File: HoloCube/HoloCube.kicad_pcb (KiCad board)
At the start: 2 copper layers, 19 parts, among them J1 ESPProgUART_RX, J3 USB_C_Receptacle_USB2.0, U1 ESP32-PICO-D4, U2 LIS2DE12, U4 XC6209

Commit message: Place Parts
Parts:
- removed D2, D4: LED, LED_SMD:LED_0603_1608Metric
- added C1: 10uf, Capacitor_SMD:C_0603_1608Metric, F.Cu at (206.5, 111.0)
- added C2: 0.1uf, Capacitor_SMD:C_0603_1608Metric, F.Cu at (211.4, 110.9)
- added C4: 0.1uf, Capacitor_SMD:C_0603_1608Metric, F.Cu at (199.5, 116.0)
- added C7: TBD, Capacitor_SMD:C_0603_1608Metric, F.Cu at (209.2, 109.0)
- added C8: 10pf, Capacitor_SMD:C_0603_1608Metric, F.Cu at (203.9, 110.1)
- added C9: TBD, Capacitor_SMD:C_0603_1608Metric, F.Cu at (201.0, 109.0)
- added J2: Conn_01x08_MountingPin, Connector_FFC-FPC:TE_0-1734839-8_1x08-1MP_P0.5mm_Horizontal, F.Cu at (215.7, 113.7)
- added J4: Micro_SD_Card, KisonNew:C91145, B.Cu at (205.3, 115.8)
- added J5: ESPProgJTAG_RX, KisonNew:IDC_1.27mm_10P, F.Cu at (193.8, 114.8)
- added JP1: Jumper, Resistor_SMD:R_0603_1608Metric, F.Cu at (199.5, 112.8)
- added JP2: Jumper, Resistor_SMD:R_0603_1608Metric, F.Cu at (199.3, 119.8)
- added R10: 10k, Resistor_SMD:R_0603_1608Metric, B.Cu at (216.4, 115.6)
- added R11: 0, Resistor_SMD:R_0603_1608Metric, B.Cu at (198.8, 124.8)
- added R12: 100k, Resistor_SMD:R_0603_1608Metric, F.Cu at (202.3, 113.2)
- added R13: 100k, Resistor_SMD:R_0603_1608Metric, F.Cu at (197.6, 119.8)
- added R14: 10k, Resistor_SMD:R_0603_1608Metric, B.Cu at (200.4, 124.8)
- added R15: 10k, Resistor_SMD:R_0603_1608Metric, B.Cu at (200.5, 128.1)
- added R16: 10k, Resistor_SMD:R_0603_1608Metric, B.Cu at (202.4, 124.8)
- added R17: 10k, Resistor_SMD:R_0603_1608Metric, B.Cu at (202.4, 128.1)
- added R2: 0, Resistor_SMD:R_0603_1608Metric, B.Cu at (195.0, 109.7)
- added R3: 0, Resistor_SMD:R_0603_1608Metric, F.Cu at (218.9, 127.7)
- added R9: 10k, Resistor_SMD:R_0603_1608Metric, F.Cu at (202.0, 120.6)
- added U3: BH1750FVI-TR, BH1750FVI-TR:XDCR_BH1750FVI-TR, F.Cu at (202.3, 118.7)
- C3, R1, R4, R6, R7: moved to B.Cu
- R5, R8: value 10k -> 3.3k; moved to B.Cu
- U2: value LIS2DE12 -> LIS2DH12TR; footprint Package_LGA:LGA-12_2x2mm_P0.5mm -> LIS2DH12TR:PQFN50P200X200100-12N
- moved D3 67.7 mm to (216.8, 120.8), turned to 180 degrees
- moved J3 66.5 mm to (208.8, 127.3)
- moved C6 66.0 mm to (218.9, 124.6), turned to -90 degrees
- moved U4 62.3 mm to (216.1, 125.1), turned to 90 degrees
- moved C5 59.4 mm to (215.8, 128.3), turned to 180 degrees
- moved R7 58.9 mm to (211.6, 126.8), turned to 90 degrees
- moved R6 54.9 mm to (206.2, 127.0), turned to 90 degrees
- moved R4 54.9 mm to (208.8, 128.6), turned to 180 degrees
- moved AE1 53.0 mm to (206.1, 107.3)
- moved R8 46.2 mm to (195.5, 122.3), turned to 180 degrees
- moved U2 46.0 mm to (202.4, 115.7), turned to 90 degrees
- moved R5 41.6 mm to (195.5, 119.8), turned to 180 degrees
- moved C3 40.3 mm to (191.7, 111.5), turned to 180 degrees
- moved R1 39.6 mm to (195.0, 111.5), turned to 180 degrees
- moved U1 38.2 mm to (208.8, 116.1)
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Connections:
- C5 pad 1: /EXT_5V -> +5V
- D1 pad 1: unconnected-(D1-Pad1) -> +5V
- D1 pad 3: unconnected-(D1-Pad3) -> GND
- D1 pad 4: unconnected-(D1-Pad4) -> /IO27
- D3 pad 1: /EXT_5V -> +5V
- J1 pad 6: unconnected-(J1-Pad6) -> /IO0
- R5 pad 1: /EXT_5V -> +3V3
- R5 pad 2: Net-(D2-Pad2) -> /I2C_SCL
- R8 pad 2: Net-(D4-Pad2) -> /I2C_SDA
- U1 pad 12: unconnected-(U1-Pad12) -> /I2C_SDA
- U1 pad 13: unconnected-(U1-Pad13) -> /I2C_SCL
- U1 pad 14: unconnected-(U1-Pad14) -> /IO25
- U1 pad 15: unconnected-(U1-Pad15) -> /IO26
- U1 pad 16: unconnected-(U1-Pad16) -> /IO27
- U1 pad 17: unconnected-(U1-Pad17) -> /TMS
- U1 pad 18: unconnected-(U1-Pad18) -> /TDI
- U1 pad 2: Net-(AE1-Pad1) -> Net-(U1-Pad2)
- U1 pad 20: unconnected-(U1-Pad20) -> /TCLK
- U1 pad 21: unconnected-(U1-Pad21) -> /TDO
- U1 pad 22: /TX -> /DC
- U1 pad 23: unconnected-(U1-Pad23) -> /IO0
- U1 pad 24: unconnected-(U1-Pad24) -> /IO4
- U1 pad 34: unconnected-(U1-Pad34) -> /IO5
- U1 pad 35: unconnected-(U1-Pad35) -> /IO18
- U1 pad 36: unconnected-(U1-Pad36) -> /IO23
- U1 pad 38: unconnected-(U1-Pad38) -> /IO19
- U1 pad 39: unconnected-(U1-Pad39) -> /IO22
- U1 pad 41: unconnected-(U1-Pad41) -> /TX
- U1 pad 42: unconnected-(U1-Pad42) -> /IO21
- U2 pad 1: unconnected-(U2-Pad1) -> /I2C_SCL
- U2 pad 10: unconnected-(U2-Pad10) -> +3V3
- U2 pad 2: unconnected-(U2-Pad2) -> +3V3
- U2 pad 3: unconnected-(U2-Pad3) -> Net-(JP1-Pad2)
- U2 pad 4: unconnected-(U2-Pad4) -> /I2C_SDA
- U2 pad 5: unconnected-(U2-Pad5) -> GND
- U2 pad 6: unconnected-(U2-Pad6) -> GND
- U2 pad 7: unconnected-(U2-Pad7) -> GND
- U2 pad 8: unconnected-(U2-Pad8) -> GND
- U2 pad 9: unconnected-(U2-Pad9) -> +3V3
- U4 pad 1: /EXT_5V -> +5V
- U4 pad 3: /EXT_5V -> +5V
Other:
- board outline added: 60.4 x 50 mm
- copper layers 2 -> 4

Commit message: Random Version 0.0
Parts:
- removed C4: 0.1uf, Capacitor_SMD:C_0603_1608Metric
- removed J5: ESPProgJTAG_RX, KisonNew:IDC_1.27mm_10P
- removed JP2: Jumper, Resistor_SMD:R_0603_1608Metric
- removed R10, R9: 10k, Resistor_SMD:R_0603_1608Metric
- removed R13: 100k, Resistor_SMD:R_0603_1608Metric
- removed R3: 0, Resistor_SMD:R_0603_1608Metric
- removed U3: BH1750FVI-TR, BH1750FVI-TR:XDCR_BH1750FVI-TR
- C2, C3, C5, C6, C7, C8, C9: footprint Capacitor_SMD:C_0603_1608Metric -> Capacitor_SMD:C_0402_1005Metric
- JP1, R1, R11, R12, R14, R15, R16, R17, R2, R4, R6, R7: footprint Resistor_SMD:R_0603_1608Metric -> Resistor_SMD:R_0402_1005Metric
- R5, R8: footprint Resistor_SMD:R_0603_1608Metric -> Resistor_SMD:R_0402_1005Metric; moved to F.Cu
- moved R17 14.0 mm to (215.5, 123.1), turned to 180 degrees
- moved J1 11.6 mm to (195.8, 114.4), turned to -90 degrees
- moved R8 11.1 mm to (203.4, 114.5), turned to -90 degrees
- moved R15 9.46 mm to (209.5, 125.3), turned to 90 degrees
- moved R5 8.35 mm to (203.3, 116.8), turned to -90 degrees
- moved C7 8.17 mm to (201.4, 111.3), turned to 0 degrees
- moved R2 8.00 mm to (193.8, 117.6), turned to 90 degrees
- moved R1 7.40 mm to (195.8, 118.9)
- moved C3 6.88 mm to (195.8, 117.0)
- moved R16 5.66 mm to (208.0, 125.4)
- moved J4 4.38 mm to (209.7, 115.5)
- moved JP1 4.25 mm to (201.0, 116.8)
- moved C5 3.68 mm to (216.8, 124.7)
- moved R12 3.60 mm to (202.1, 116.8), turned to -90 degrees
- moved C6 2.79 mm to (218.7, 127.3), turned to 90 degrees
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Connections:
- AE1 pad 2: (no net) -> GND
- C1 pad 1: +3.3VA -> +3V3
- C2 pad 1: +3.3VA -> +3V3
- D1 pad 4: /IO27 -> /IO19
- J2 pad 1: /IO5 -> /IO22
- J2 pad 3: /IO23 -> /IO5
- J4 pad 2: /IO21 -> /IO15
- J4 pad 3: /IO25 -> /IO13
- J4 pad 5: /IO19 -> /IO26
- J4 pad 7: /IO26 -> /IO25
- R14 pad 2: /IO26 -> /IO25
- R15 pad 2: /IO25 -> /IO13
- R16 pad 2: /IO19 -> /IO26
- R17 pad 2: /IO21 -> /IO15
- R2 pad 1: Net-(J1-Pad2) -> +3V3
- R2 pad 2: +3V3 -> Net-(J1-Pad2)
- U1 pad 1: +3.3VA -> +3V3
- U1 pad 18: /TDI -> /IO12
- U1 pad 19: +3.3VA -> +3V3
- U1 pad 20: /TCLK -> /IO13
- U1 pad 21: /TDO -> /IO15
- U1 pad 22: /DC -> unconnected-(U1-Pad22)
- U1 pad 3: +3.3VA -> +3V3
- U1 pad 36: /IO23 -> /DC
- U1 pad 37: +3.3VA -> +3V3
- U1 pad 4: +3.3VA -> +3V3
- U1 pad 42: /IO21 -> unconnected-(U1-Pad42)
- U1 pad 43: +3.3VA -> +3V3
- U1 pad 46: +3.3VA -> +3V3
- U2 pad 6: GND -> unconnected-(U2-Pad6)
- U2 pad 7: GND -> unconnected-(U2-Pad7)
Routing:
- net +3V3: track 0.00 -> 99.4 mm, vias 0 -> 9
- net GND: track 0.00 -> 73.0 mm, vias 0 -> 11
- net +5V: track 0.00 -> 52.4 mm, vias 0 -> 2
- net /IO0: track 0.00 -> 25.7 mm, vias 0 -> 2
- net /IO19: track 0.00 -> 24.2 mm, vias 0 -> 2
- net Net-(D3-Pad2): track 0.00 -> 23.7 mm, vias 0 -> 2
- net Net-(J3-PadS1): track 0.00 -> 18.4 mm
- net /RX: track 0.00 -> 17.1 mm, vias 0 -> 2
- net /IO22: track 0.00 -> 15.4 mm, vias 0 -> 2
- net /TX: track 0.00 -> 15.0 mm, vias 0 -> 2
- net /EN: track 0.00 -> 14.5 mm, vias 0 -> 2
- net /I2C_SCL: track 0.00 -> 9.69 mm
- net /IO15: track 0.00 -> 7.84 mm, vias 0 -> 1
- net Net-(AE1-Pad1): track 0.00 -> 7.36 mm
- net /IO4: track 0.00 -> 7.13 mm
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- added copper zone on B.Cu, net GND
- added copper zone on F.Cu, net GND
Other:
- board outline removed

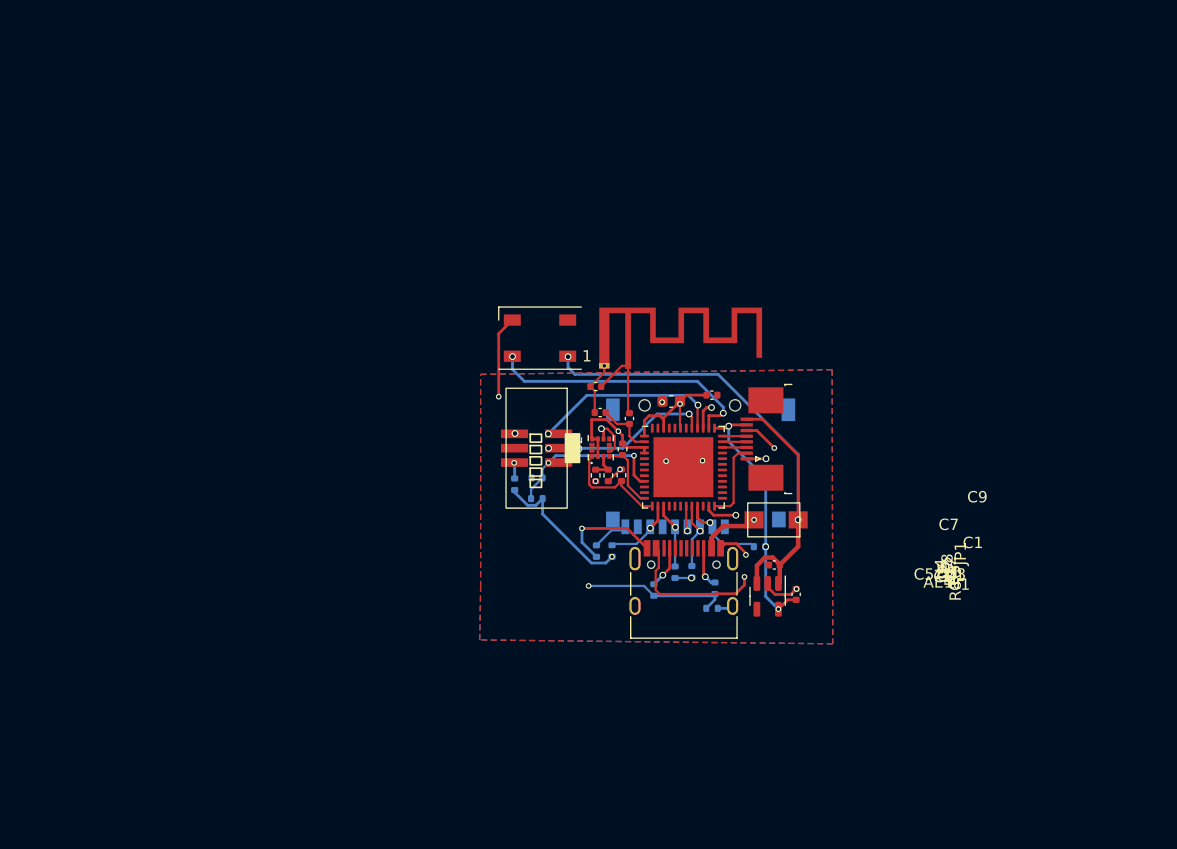
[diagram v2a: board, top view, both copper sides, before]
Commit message: Improve According to t123yh
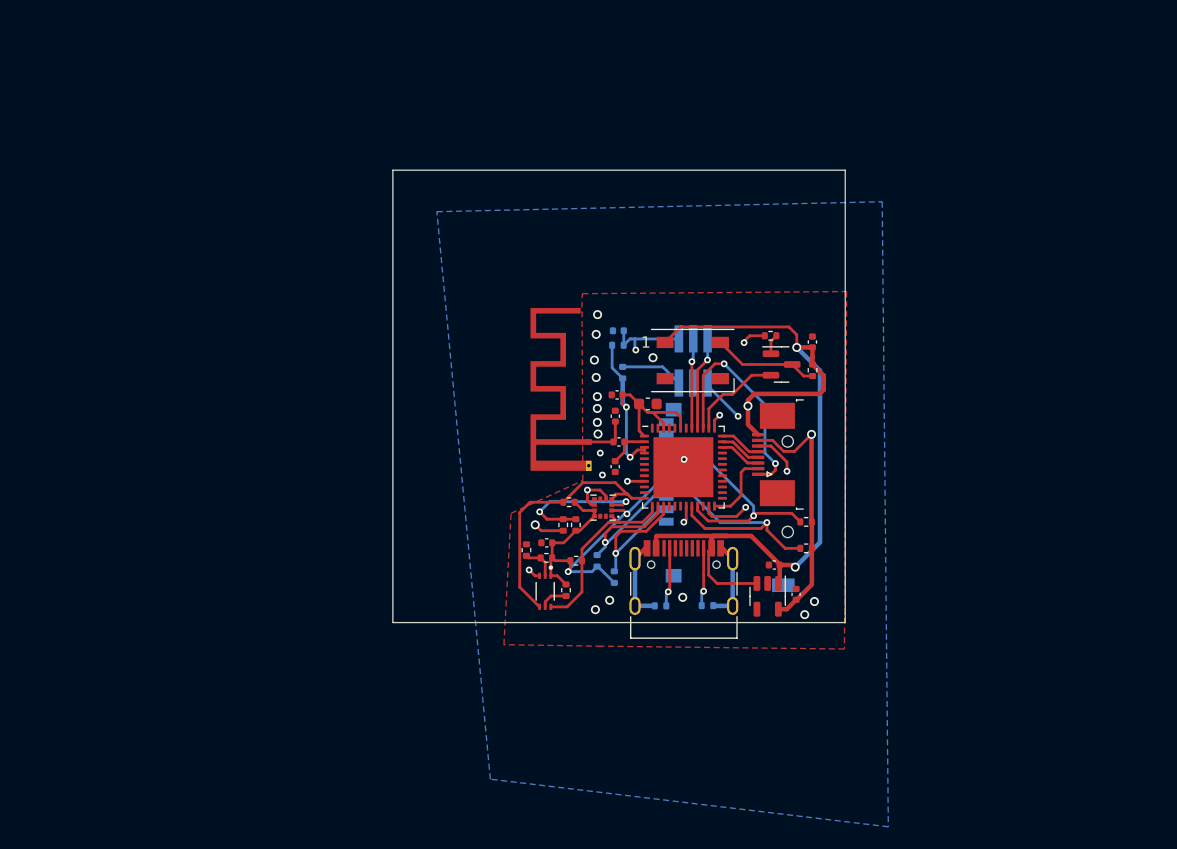
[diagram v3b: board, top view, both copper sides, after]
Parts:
- removed D3: D, KisonNew:C8678
- removed R11: 0, Resistor_SMD:R_0402_1005Metric
- added C10: 0.1uF, Capacitor_SMD:C_0402_1005Metric, F.Cu at (220.2, 105.0)
- added C4: 0.1uf, Capacitor_SMD:C_0402_1005Metric, F.Cu at (196.7, 122.8)
- added JP2: Jumper, Resistor_SMD:R_0402_1005Metric, F.Cu at (196.7, 124.1)
- added Q1: MMBT3904, Package_TO_SOT_SMD:SOT-23, F.Cu at (217.4, 107.0)
- added R10: 10k, Resistor_SMD:R_0402_1005Metric, F.Cu at (220.2, 107.5)
- added R3: 10k, Resistor_SMD:R_0402_1005Metric, F.Cu at (198.4, 127.0)
- added R9: 100k, Resistor_SMD:R_0402_1005Metric, F.Cu at (194.9, 123.4)
- added U3: BH1750FVI-TR, BH1750FVI-TR:XDCR_BH1750FVI-TR, F.Cu at (196.5, 127.1)
- J1: moved to B.Cu
- R14, R16: moved to F.Cu
- R4: value 0 -> 1.5k; moved to F.Cu
- moved R4 24.7 mm to (216.5, 104.5)
- moved R14 17.4 mm to (219.6, 120.9), turned to 180 degrees
- moved J1 15.9 mm to (209.6, 106.7), turned to 180 degrees
- moved R1 15.3 mm to (203.0, 105.3), turned to 0 degrees
- moved C3 14.9 mm to (203.0, 104.0)
- moved R2 13.7 mm to (203.4, 107.7)
- moved D1 13.7 mm to (209.6, 106.7), turned to 0 degrees
- moved R17 13.1 mm to (202.7, 125.8), turned to 90 degrees
- moved R16 11.8 mm to (219.6, 123.3), turned to 180 degrees
- moved R5 8.55 mm to (199.3, 124.4), turned to 0 degrees
- moved R15 8.44 mm to (201.1, 124.4)
- moved C2 8.38 mm to (202.9, 109.7), turned to 180 degrees
- moved AE1 7.58 mm to (200.4, 113.9), turned to 90 degrees
- moved R8 6.65 mm to (198.7, 119.2), turned to 180 degrees
- moved U2 5.31 mm to (201.7, 119.7), turned to 180 degrees
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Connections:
- D1 pad 4: /IO19 -> Net-(D1-Pad4)
- J3 pad A4: Net-(D3-Pad2) -> +5V
- J3 pad A9: Net-(D3-Pad2) -> +5V
- J3 pad B4: Net-(D3-Pad2) -> +5V
- J3 pad B9: Net-(D3-Pad2) -> +5V
- J3 pad S1: Net-(J3-PadS1) -> GND
- J4 pad 2: /IO15 -> /IO26
- J4 pad 3: /IO13 -> /IO25
- J4 pad 5: /IO26 -> /IO13
- J4 pad 7: /IO25 -> /IO15
- J4 pad 9: Net-(J4-Pad9) -> GND
- R14 pad 2: /IO25 -> /IO15
- R15 pad 2: /IO13 -> /IO25
- R16 pad 2: /IO26 -> /IO13
- R17 pad 2: /IO15 -> /IO26
- R4 pad 1: Net-(J3-PadS1) -> Net-(Q1-Pad1)
- R4 pad 2: GND -> +3V3
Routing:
- net GND: track 73.0 -> 26.4 mm, vias 11 -> 21
- net +3V3: track 99.4 -> 132.9 mm, vias 9 -> 8
- net +5V: track 52.4 -> 76.6 mm, vias 2 -> 3
- net Net-(D3-Pad2): track 23.7 -> 0.00 mm, vias 2 -> 0
- net Net-(J3-PadS1): track 18.4 -> 0.00 mm
- net /I2C_SDA: track 6.05 -> 23.4 mm
- net /IO13: track 5.89 -> 23.2 mm
- net /IO19: track 24.2 -> 8.44 mm, vias 2 -> 0
- net /IO15: track 7.84 -> 21.2 mm
- net Net-(JP1-Pad2): track 2.47 -> 12.9 mm, vias 0 -> 2
- net Net-(D1-Pad4): track 0.00 -> 9.37 mm
- net /IO26: track 5.77 -> 15.1 mm
- net /IO25: track 6.33 -> 15.4 mm
- net /IO0: track 25.7 -> 16.8 mm
- net /RX: track 17.1 -> 8.26 mm, vias 2 -> 1
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- added copper zone on In1.Cu, net GND
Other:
- board outline added: 40 x 40 mm
- board text added: "emm这玩意怎么铺铜的时候连上2脚啊，因为天线的net2脚设为GND也铺不到"
- board text added: "朝向用户"
- board text added: "这边是屁股，记得机械在光传感器上留出透明位置"

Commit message: Improve again
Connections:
- J2 pad MP: unconnected-(J2-PadMP) -> GND
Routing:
- net GND: track 26.4 -> 31.4 mm, vias 21 -> 25

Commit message: V0.1
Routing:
- net GND: vias 25 -> 27
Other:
- board size 40 x 40 mm -> 30 x 29 mm
- board text added: "定位孔相距16mm,右边孔相距上下左右边线2mm"
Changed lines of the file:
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@@
     )
   )
-  (gr_line (start 183.07 129.83) (end 223.07 129.83) (layer "Edge.Cuts") (width 0.1))
-  (gr_line (start 223.07 89.83) (end 223.07 129.83) (layer "Edge.Cuts") (width 0.1))
-  (gr_line (start 223.07 89.83) (end 183.07 89.83) (layer "Edge.Cuts") (width 0.1))
-  (gr_line (start 183.07 129.83) (end 183.07 89.83) (layer "Edge.Cuts") (width 0.1))
+  (gr_line (start 194.57 129.79) (end 221.57 129.79) (layer "Edge.Cuts") (width 0.1))
+  (gr_arc (start 221.57 100.79) (mid 222.63066 101.22934) (end 223.07 102.29) (layer "Edge.Cuts") (width 0.1))
+  (gr_arc (start 194.57 129.79) (mid 193.50934 129.35066) (end 193.07 128.29) (layer "Edge.Cuts") (width 0.1))
+  (gr_line (start 193.07 128.29) (end 193.07 102.29) (layer "Edge.Cuts") (width 0.1))
+  (gr_line (start 223.07 102.29) (end 223.07 128.29) (layer "Edge.Cuts") (width 0.1))
+  (gr_arc (start 223.07 128.29) (mid 222.63066 129.35066) (end 221.57 129.79) (layer "Edge.Cuts") (width 0.1))
+  (gr_arc (start 193.07 102.29) (mid 193.50934 101.22934) (end 194.57 100.79) (layer "Edge.Cuts") (width 0.1))
+  (gr_line (start 221.57 100.79) (end 194.57 100.79) (layer "Edge.Cuts") (width 0.1))
   (gr_text "这边是屁股，记得机械在光传感器上留出透明位置" (at 208.71 134.04) (layer "Cmts.User")
     (effects (font (size 1 1) (thickness 0.15)))
@@
   (gr_text "朝向用户" (at 208.91 99.25) (layer "Cmts.User")
     (effects (font (size 1 1) (thickness 0.15)))
+  )
+  (gr_text "定位孔相距16mm,右边孔相距上下左右边线2mm" (at 211.52 96.33) (layer "Cmts.User")
+    (effects (font (size 1.5 1.5) (thickness 0.3)))
   )
   (gr_text "emm这玩意怎么铺铜的时候连上2脚啊，因为天线的net2脚设为GND也铺不到" (at 201.98 88.91) (layer "Cmts.User")
@@
   (segment (start 201.6 116.78) (end 201.21 116.78) (width 0.6) (layer "F.Cu") (net 3))
   (via (at 208.7 127.6) (size 0.8) (drill 0.5) (layers "F.Cu" "B.Cu") (free) (net 3))
+  (via (at 221.07 102.79) (size 1.5) (drill 1) (layers "F.Cu" "B.Cu") (free) (net 3))
   (via (at 201.15 112.13) (size 0.8) (drill 0.5) (layers "F.Cu" "B.Cu") (free) (net 3))
   (via (at 217.92 116.45) (size 0.6) (drill 0.3) (layers "F.Cu" "B.Cu") (net 3))
@@
   (via (at 208.82 115.4) (size 0.6) (drill 0.3) (layers "F.Cu" "B.Cu") (net 3))
   (via (at 201.05 104.35) (size 0.8) (drill 0.5) (layers "F.Cu" "B.Cu") (free) (net 3))
+  (via (at 205.07 102.79) (size 1.5) (drill 1) (layers "F.Cu" "B.Cu") (free) (net 3))
   (via (at 210.7184 117.5512) (size 0.8) (drill 0.5) (layers "F.Cu" "B.Cu") (net 3))
   (via (at 201.15 110.9) (size 0.8) (drill 0.5) (layers "F.Cu" "B.Cu") (free) (net 3))
@@
   (segment (start 202.75 118.5925) (end 202.4225 118.92) (width 0.25) (layer "F.Cu") (net 16))
   (segment (start 203.76 118.47) (end 203.832482 118.47) (width 0.25) (layer "F.Cu") (net 16))
+  (segment (start 196.04 127.65904) (end 194.28548 125.90452) (width 0.25) (layer "F.Cu") (net 16))
   (segment (start 202.75 118.47) (end 202.75 118.5925) (width 0.25) (layer "F.Cu") (net 16))
+  (segment (start 196.04 128.445) (end 196.04 127.65904) (width 0.25) (layer "F.Cu") (net 16))
   (segment (start 203.832482 118.47) (end 204.202482 118.84) (width 0.25) (layer "F.Cu") (net 16))
   (segment (start 194.28548 120.10452) (end 195.2 119.19) (width 0.25) (layer "F.Cu") (net 16))
   (segment (start 195.2 119.19) (end 198.14 119.19) (width 0.25) (layer "F.Cu") (net 16))
+  (segment (start 194.28548 125.90452) (end 194.28548 120.10452) (width 0.25) (layer "F.Cu") (net 16))
   (segment (start 204.202482 118.84) (end 205.31 118.84) (width 0.25) (layer "F.Cu") (net 16))
-  (segment (start 196.04 128.445) (end 194.28548 126.69048) (width 0.25) (layer "F.Cu") (net 16))
   (segment (start 198.14 119.19) (end 199.87 117.46) (width 0.25) (layer "F.Cu") (net 16))
   (segment (start 202.75 117.46) (end 203.76 118.47) (width 0.25) (layer "F.Cu") (net 16))
-  (segment (start 194.28548 126.69048) (end 194.28548 120.10452) (width 0.25) (layer "F.Cu") (net 16))
   (segment (start 203.832482 118.47) (end 202.75 118.47) (width 0.25) (layer "F.Cu") (net 16))
   (segment (start 199.87 117.46) (end 202.75 117.46) (width 0.25) (layer "F.Cu") (net 16))
@@
         (xy 201.51 131.92)
         (xy 192.89 131.79)
-        (xy 193.52 120.17)
+        (xy 192.83 120.19)
         (xy 199.87 117.27)
         (xy 199.79 101.08)
